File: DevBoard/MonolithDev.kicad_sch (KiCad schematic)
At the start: 4 parts

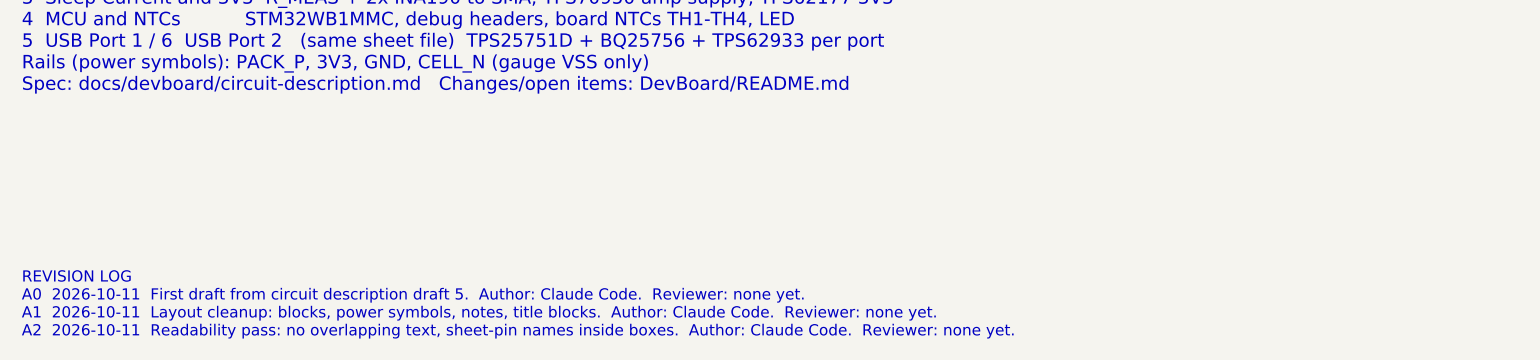
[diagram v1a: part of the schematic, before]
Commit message: Dev board rev A4: design-review fixes, polymer bulk, charge inhibit
Schematic design review (three reviewers, cross-challenged) in
docs/devboard/schematic-review-2026-10-12.md, and its fixes:
- U203 TPS70950 EN no longer tied to PACK_P (would destroy it)
- ICHG 17.8k: 2.8 A per port (was 9.8 A, above the cells' 5.6 A)
- U101 footprint from TI RSM0032A (1.4 mm thermal pad, was 2.8 mm)
- D+/D- ESD now 5 V PESD5V0S2BT (TPS25751 GPIO4/5 are rated 6 V)
- R101-R104 1206, F101 and J101 DNP, DNP gate parts on Q102
- BTP_INT buffered by a 2N7002; SMBus pull-ups on a removable 0R
- Wake button, bench PACK_P header, reset, BOOT0/3V3_SLEEP pads,
  J303 series resistors, IRQ pull-ups, vertical SMAs, BOM ratings

Open-question decisions: CHG_INH (PB8 -> each BQ25756 CE) lets the
MCU stop charging independently of the TPS25751; J103 in EV2400
SMBus pin order; "fit cells before USB" silkscreen.

Charger bulk banks now one solid polymer cap plus the MLCCs at the
FETs (16 fewer MLCCs). PWR_FLAGs moved to where each rail is sourced.
Board: footprints swapped/added and placed, DRC clean before routing.

Co-Authored-By: Claude Opus 5.5 <noreply@anthropic.com>
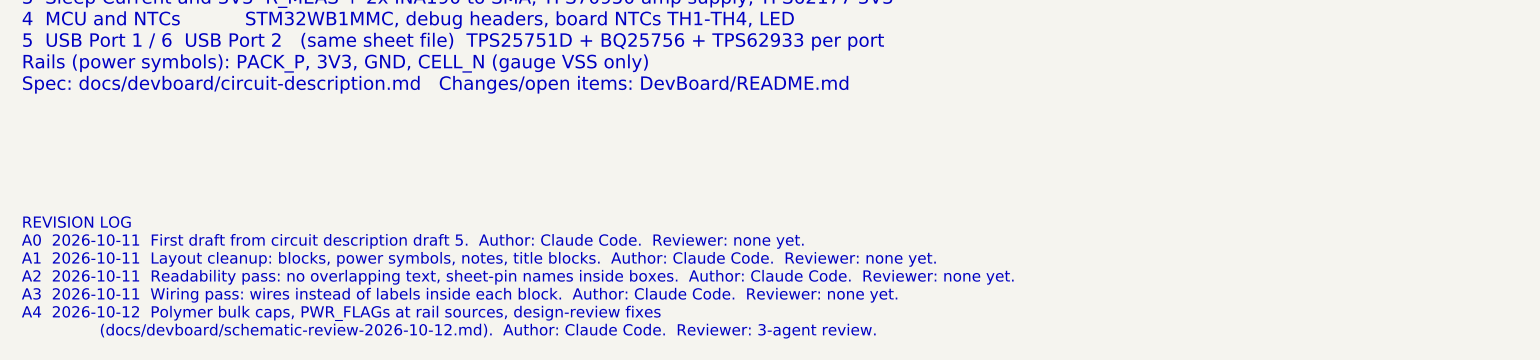
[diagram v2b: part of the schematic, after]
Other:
- note added: "REVISION LOG A0 2026-10-11 First draft from circuit description draft 5. Author: Claude Code. Reviewer: none yet. A1 2026-10-11 Layout cleanup: blocks, power symbols, notes, title blocks. Author: Claude Code. Reviewer: none yet. A2 2026-10-11 Readability pass: no overlapping text, sheet-pin names inside boxes. Author: Claude Code. Reviewer: none yet. A3 2026-10-11 Wiring pass: wires instead of la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"
- note removed: "REVISION LOG A0 2026-10-11 First draft from circuit description draft 5. Author: Claude Code. Reviewer: none yet. A1 2026-10-11 Layout cleanup: blocks, power symbols, notes, title blocks. Author: Claude Code. Reviewer: none yet. A2 2026-10-11 Readability pass: no overlapping text, sheet-pin names inside boxes. Author: Claude Code. Reviewer: none yet."
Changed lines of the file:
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@@
 		)
 	)
-	(text "REVISION LOG\nA0  2026-10-11  First draft from circuit description draft 5.  Author: Claude Code.  Reviewer: none yet.\nA1  2026-10-11  Layout cleanup: blocks, power symbols, notes, title blocks.  Author: Claude Code.  Reviewer: none yet.\nA2  2026-10-11  Readability pass: no overlapping text, sheet-pin names inside boxes.  Author: Claude Code.  Reviewer: none yet."
+	(text "REVISION LOG\nA0  2026-10-11  First draft from circuit description draft 5.  Author: Claude Code.  Reviewer: none yet.\nA1  2026-10-11  Layout cleanup: blocks, power symbols, notes, title blocks.  Author: Claude Code.  Reviewer: none yet.\nA2  2026-10-11  Readability pass: no overlapping text, sheet-pin names inside boxes.  Author: Claude Code.  Reviewer: none yet.\nA3  2026-10-11  Wiring pass: wires instead of labels inside each block.  Author: Claude Code.  Reviewer: none yet.\nA4  2026-10-12  Polymer bulk caps, PWR_FLAGs at rail sources, design-review fixes\n                (docs/devboard/schematic-review-2026-10-12.md).  Author: Claude Code.  Reviewer: 3-agent review."
 		(exclude_from_sim no)
 		(at 30.48 233.68 0)

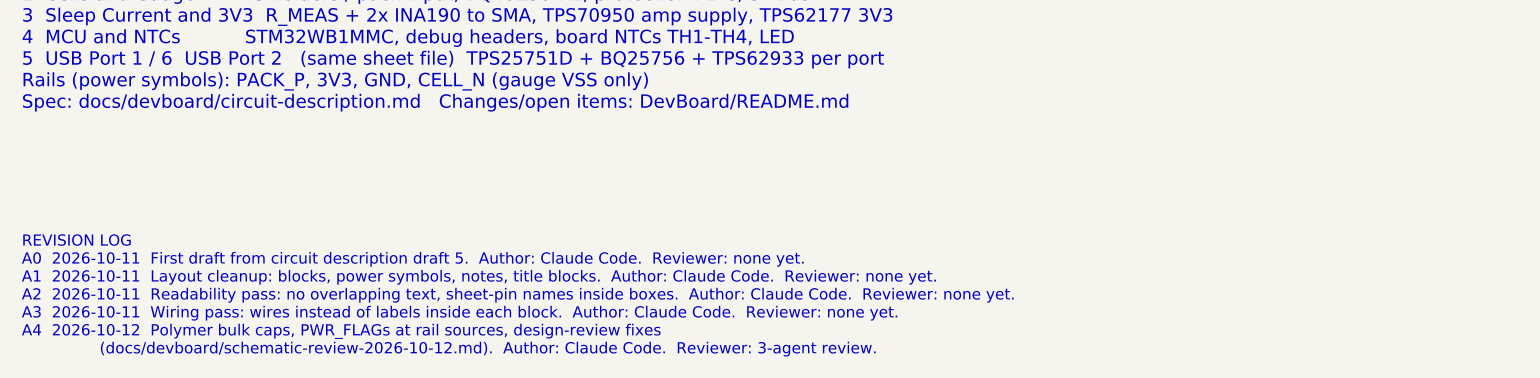
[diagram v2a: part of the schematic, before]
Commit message: Dev board rev A5: FET ESD caps, review 2, fail-safe CHG_INH, MCU I/O plan
- Gauge: C110/C111 (2 x 0.1 uF in series) across the protection FET pair,
  TI BQ40Z50-R2 fig. 9-2 C1/C2; C107/C108 across PACK+/PACK- unchanged.
- Second 3-reviewer schematic review with a challenge round
  (docs/devboard/schematic-review-2-2026-10-12.md, raw files in review2/):
  0 critical, 1 major (gauge precharge config), hardware proposals listed.
- CHG_INH now fails safe: R417/R517 47k pull-up on CE to 3V3; the MCU
  drives PB8 low to allow charging. MCU IWDG in hardware mode.
- Decisions: ICHG stays 9.1k; F101 stays 15 A with a gauge cut-off of
  2.8 V/cell or higher under load.
- docs/devboard/mcu-io-power-states.md: every MCU pin per power state,
  reconciled with the 150 uA sleep budget (PB8 low only while charging).

Co-Authored-By: Claude Opus 5.5 <noreply@anthropic.com>
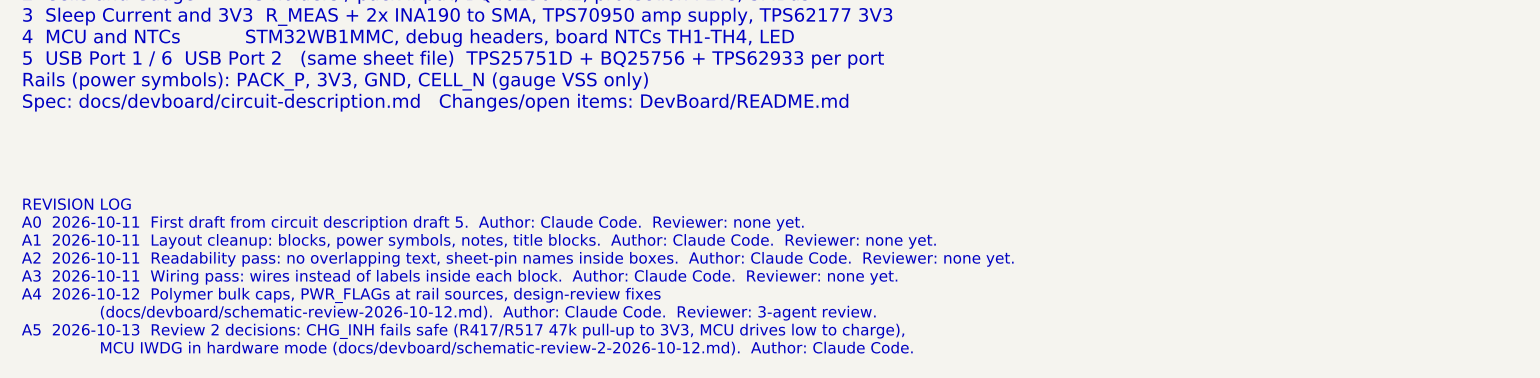
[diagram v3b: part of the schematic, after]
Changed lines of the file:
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@@
 		)
 	)
-	(text "REVISION LOG\nA0  2026-10-11  First draft from circuit description draft 5.  Author: Claude Code.  Reviewer: none yet.\nA1  2026-10-11  Layout cleanup: blocks, power symbols, notes, title blocks.  Author: Claude Code.  Reviewer: none yet.\nA2  2026-10-11  Readability pass: no overlapping text, sheet-pin names inside boxes.  Author: Claude Code.  Reviewer: none yet.\nA3  2026-10-11  Wiring pass: wires instead of labels inside each block.  Author: Claude Code.  Reviewer: none yet.\nA4  2026-10-12  Polymer bulk caps, PWR_FLAGs at rail sources, design-review fixes\n                (docs/devboard/schematic-review-2026-10-12.md).  Author: Claude Code.  Reviewer: 3-agent review."
+	(text "REVISION LOG\nA0  2026-10-11  First draft from circuit description draft 5.  Author: Claude Code.  Reviewer: none yet.\nA1  2026-10-11  Layout cleanup: blocks, power symbols, notes, title blocks.  Author: Claude Code.  Reviewer: none yet.\nA2  2026-10-11  Readability pass: no overlapping text, sheet-pin names inside boxes.  Author: Claude Code.  Reviewer: none yet.\nA3  2026-10-11  Wiring pass: wires instead of labels inside each block.  Author: Claude Code.  Reviewer: none yet.\nA4  2026-10-12  Polymer bulk caps, PWR_FLAGs at rail sources, design-review fixes\n                (docs/devboard/schematic-review-2026-10-12.md).  Author: Claude Code.  Reviewer: 3-agent review.\nA5  2026-10-13  Review 2 decisions: CHG_INH fails safe (R417/R517 47k pull-up to 3V3, MCU drives low to charge),\n                MCU IWDG in hardware mode (docs/devboard/schematic-review-2-2026-10-12.md).  Author: Claude Code."
 		(exclude_from_sim no)
 		(at 30.48 233.68 0)

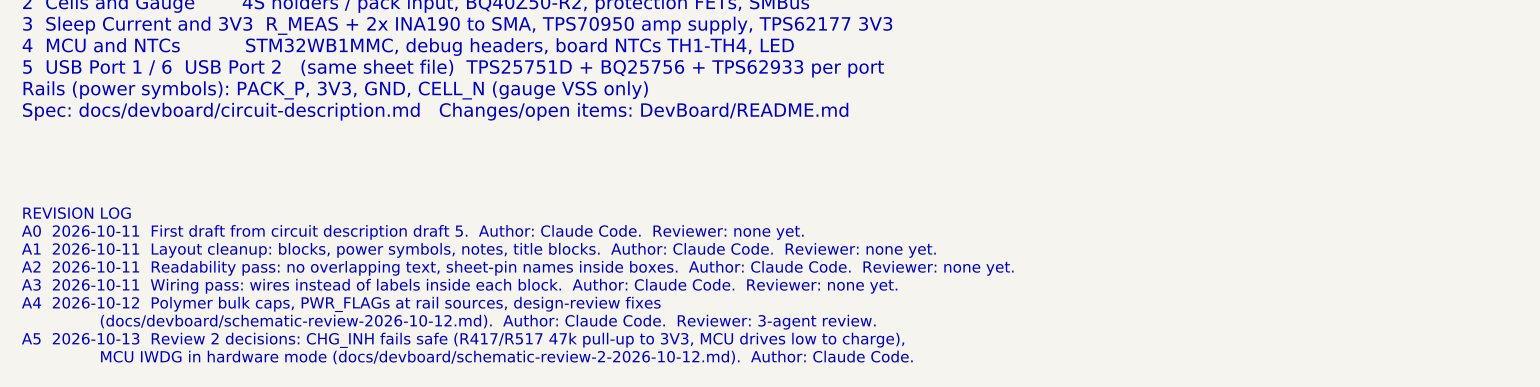
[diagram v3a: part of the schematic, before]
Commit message: Dev board rev A5: BAT fed before F101, review 2 hardware fixes, JLC passives
- Gauge BAT feed follows TI fig. 9-12: D101 from the cell top (CELL_P_RAW)
  before F101, so the gauge stays powered if the fuse opens or is unfitted.
- C421/C521 100 uF 35 V polymer (same 6.3 mm footprint): about 99 uF worst
  case vs the BQ25756 80 uF minimum after derating.
- Bootstrap diodes LRB520S-40T1G, Q103 BSS138, DNP C109 4.7 nF (fit D103
  with it), PPHV 0.1 uF and VBUS 10 nF per port, R306 330R, C201 DNP flag.
- Test points: GND loops by each port's SW probes and in the pack probe
  field, CELL_P_RAW, CE_N, LDO_3V3, LDO_IN, 5V_AMP.
- JLC part numbers on every resistor and capacitor.
- Placement for the new parts; placer hides test-point labels with no
  free spot. DRC clean, schematic parity clean.

Co-Authored-By: Claude Opus 5.5 <noreply@anthropic.com>
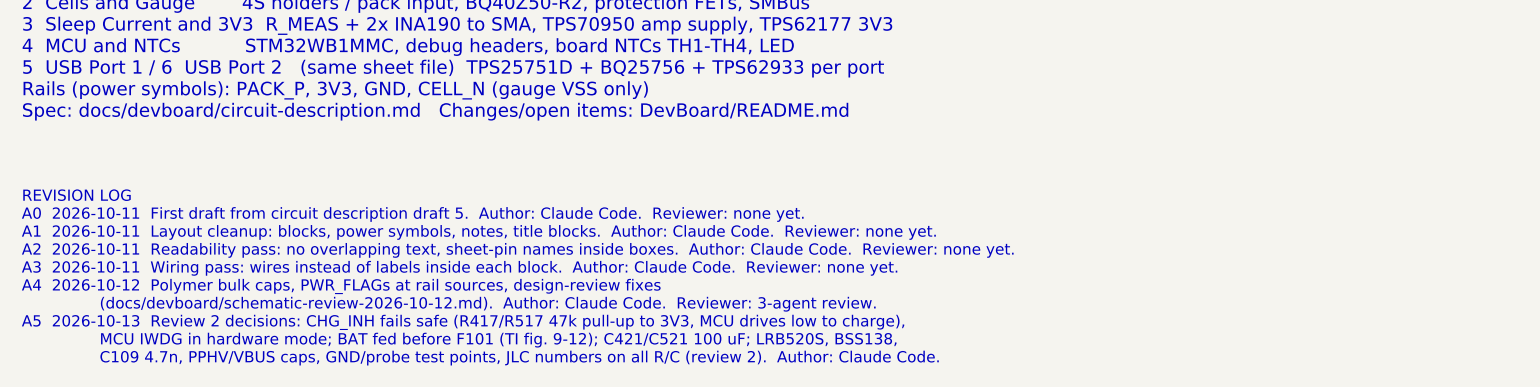
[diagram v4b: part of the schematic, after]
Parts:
- R1, R2, R3, R4: LCSC (none) -> C21189; MPN (none) -> 0603WAF0000T5E
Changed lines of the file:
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@@
 		)
 	)
-	(text "REVISION LOG\nA0  2026-10-11  First draft from circuit description draft 5.  Author: Claude Code.  Reviewer: none yet.\nA1  2026-10-11  Layout cleanup: blocks, power symbols, notes, title blocks.  Author: Claude Code.  Reviewer: none yet.\nA2  2026-10-11  Readability pass: no overlapping text, sheet-pin names inside boxes.  Author: Claude Code.  Reviewer: none yet.\nA3  2026-10-11  Wiring pass: wires instead of labels inside each block.  Author: Claude Code.  Reviewer: none yet.\nA4  2026-10-12  Polymer bulk caps, PWR_FLAGs at rail sources, design-review fixes\n                (docs/devboard/schematic-review-2026-10-12.md).  Author: Claude Code.  Reviewer: 3-agent review.\nA5  2026-10-13  Review 2 decisions: CHG_INH fails safe (R417/R517 47k pull-up to 3V3, MCU drives low to charge),\n                MCU IWDG in hardware mode (docs/devboard/schematic-review-2-2026-10-12.md).  Author: Claude Code."
+	(text "REVISION LOG\nA0  2026-10-11  First draft from circuit description draft 5.  Author: Claude Code.  Reviewer: none yet.\nA1  2026-10-11  Layout cleanup: blocks, power symbols, notes, title blocks.  Author: Claude Code.  Reviewer: none yet.\nA2  2026-10-11  Readability pass: no overlapping text, sheet-pin names inside boxes.  Author: Claude Code.  Reviewer: none yet.\nA3  2026-10-11  Wiring pass: wires instead of labels inside each block.  Author: Claude Code.  Reviewer: none yet.\nA4  2026-10-12  Polymer bulk caps, PWR_FLAGs at rail sources, design-review fixes\n                (docs/devboard/schematic-review-2026-10-12.md).  Author: Claude Code.  Reviewer: 3-agent review.\nA5  2026-10-13  Review 2 decisions: CHG_INH fails safe (R417/R517 47k pull-up to 3V3, MCU drives low to charge),\n                MCU IWDG in hardware mode; BAT fed before F101 (TI fig. 9-12); C421/C521 100 uF; LRB520S, BSS138,\n                C109 4.7n, PPHV/VBUS caps, GND/probe test points, JLC numbers on all R/C (review 2).  Author: Claude Code."
 		(exclude_from_sim no)
 		(at 30.48 233.68 0)
@@
 			)
 		)
+		(property "LCSC" "C21189"
+			(at 116.84 160.02 0)
+			(hide yes)
+			(show_name no)
+			(do_not_autoplace no)
+			(effects
+				(font
+					(size 1.27 1.27)
+				)
+			)
+		)
+		(property "MPN" "0603WAF0000T5E"
+			(at 116.84 160.02 0)
+			(hide yes)
+			(show_name no)
+			(do_not_autoplace no)
+			(effects
+				(font
+					(size 1.27 1.27)
+				)
+			)
+		)
 		(pin "1"
 		)
@@
 			)
 		)
+		(property "LCSC" "C21189"
+			(at 254 160.02 0)
+			(hide yes)
+			(show_name no)
+			(do_not_autoplace no)
+			(effects
+				(font
+					(size 1.27 1.27)
+				)
+			)
+		)
+		(property "MPN" "0603WAF0000T5E"
+			(at 254 160.02 0)
+			(hide yes)
+			(show_name no)
+			(do_not_autoplace no)
+			(effects
+				(font
+					(size 1.27 1.27)
+				)
+			)
+		)
 		(pin "1"
 		)
@@
 			)
 		)
+		(property "LCSC" "C21189"
+			(at 129.54 160.02 0)
+			(hide yes)
+			(show_name no)
+			(do_not_autoplace no)
+			(effects
+				(font
+					(size 1.27 1.27)
+				)
+			)
+		)
+		(property "MPN" "0603WAF0000T5E"
+			(at 129.54 160.02 0)
+			(hide yes)
+			(show_name no)
+			(do_not_autoplace no)
+			(effects
+				(font
+					(size 1.27 1.27)
+				)
+			)
+		)
 		(pin "1"
 		)
@@
 			(hide yes)
 			(show_name no)
+			(do_not_autoplace no)
+			(effects
+				(font
+					(size 1.27 1.27)
+				)
+			)
+		)
+		(property "LCSC" "C21189"
+			(at 241.3 160.02 0)
+			(hide yes)
+			(show_name no)
+			(do_not_autoplace no)
+			(effects
+				(font
+					(size 1.27 1.27)
+				)
+			)
+		)
+		(property "MPN" "0603WAF0000T5E"
+			(at 241.3 160.02 0)
+			(hide yes)
+			(show_name no)
